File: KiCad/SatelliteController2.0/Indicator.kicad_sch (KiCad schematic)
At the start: 38 parts

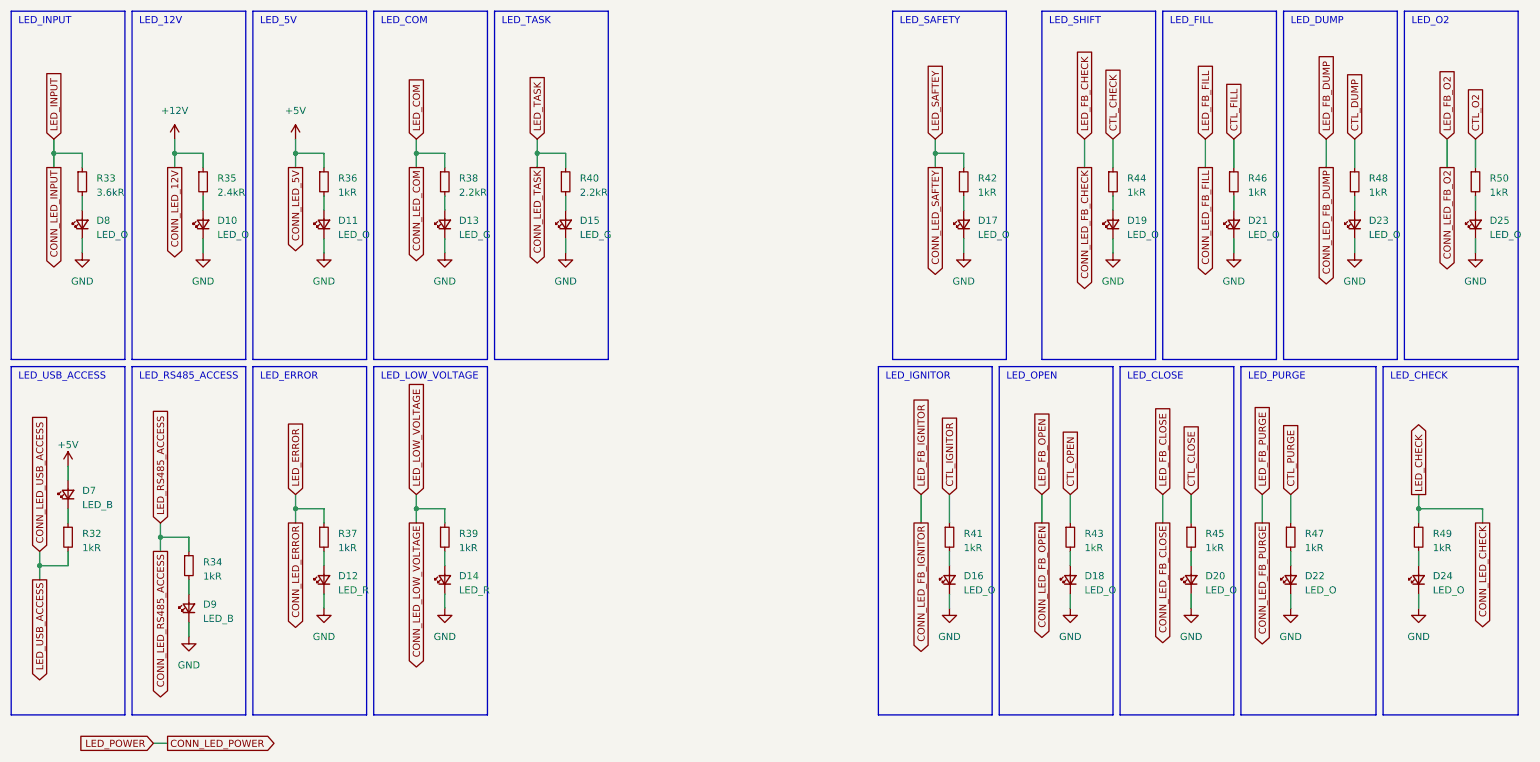
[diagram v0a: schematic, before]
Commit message: シルクなどを調整
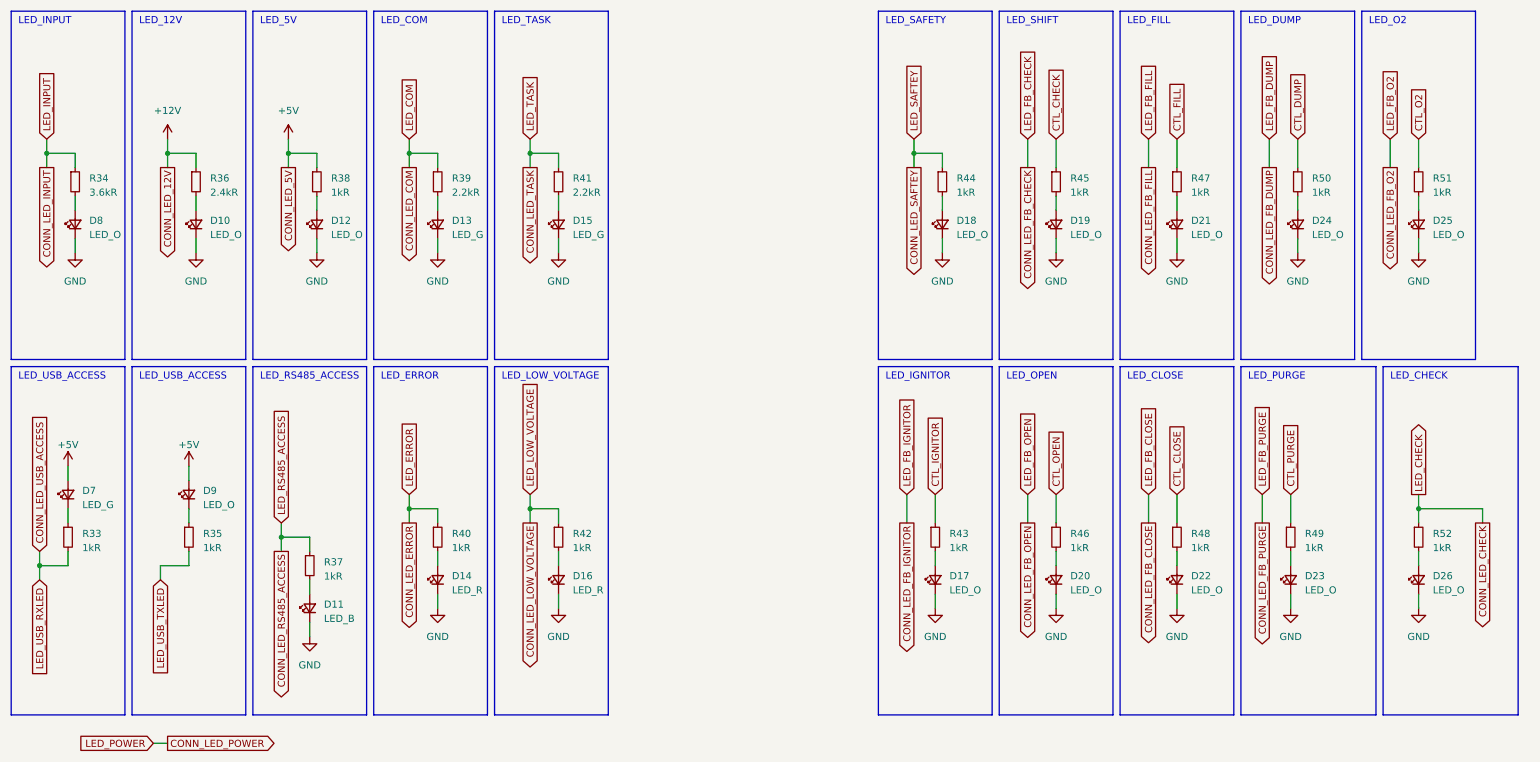
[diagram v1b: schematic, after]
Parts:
- added D9: LED_O, LED_SMD:LED_0603_1608Metric_Pad1.05x0.95mm_HandSolder, symbol Device:LED_Small
- added R35: 1kR, Resistor_SMD:R_0603_1608Metric_Pad0.98x0.95mm_HandSolder, symbol Device:R_Small
- D10, D19, D21, D25, D8: Digikey_PN (none) -> SML-D12D8WT86CCT-ND
- D11: renamed from D9; Digikey_PN (none) -> SMLD12BN1WT86CT-ND
- D12: renamed from D11; Digikey_PN (none) -> SML-D12D8WT86CCT-ND
- D13, D15: Digikey_PN (none) -> SML-D12P8WT86CCT-ND
- D14: renamed from D12; Digikey_PN (none) -> SML-D12U8WT86CCT-ND
- D16: renamed from D14; Digikey_PN (none) -> SML-D12U8WT86CCT-ND
- D17: renamed from D16; Digikey_PN (none) -> SML-D12D8WT86CCT-ND
- D18: renamed from D17; Digikey_PN (none) -> SML-D12D8WT86CCT-ND
- D20: renamed from D18; Digikey_PN (none) -> SML-D12D8WT86CCT-ND
- D22: renamed from D20; Digikey_PN (none) -> SML-D12D8WT86CCT-ND
- D23: renamed from D22; Digikey_PN (none) -> SML-D12D8WT86CCT-ND
- D24: renamed from D23; Digikey_PN (none) -> SML-D12D8WT86CCT-ND
- D26: renamed from D24; Digikey_PN (none) -> SML-D12D8WT86CCT-ND
- D7: value LED_B -> LED_G; Digikey_PN (none) -> SML-D12P8WT86CCT-ND
- R33: renamed from R32; Digikey_PN (none) -> 2019-RK73H1JTTD1001FCT-ND
- R34: renamed from R33; Digikey_PN (none) -> 2019-RK73H1JTTD3601FCT-ND
- R36: renamed from R35; Digikey_PN (none) -> 2019-RK73H1JTTD2401FCT-ND
- R37: renamed from R34; Digikey_PN (none) -> 2019-RK73H1JTTD1001FCT-ND
- R38: renamed from R36; Digikey_PN (none) -> 2019-RK73H1JTTD1001FCT-ND
- R39: renamed from R38; Digikey_PN (none) -> 2019-RK73H1JTTD2201FCT-ND
- R40: renamed from R37; Digikey_PN (none) -> 2019-RK73H1JTTD1001FCT-ND
- R41: renamed from R40; Digikey_PN (none) -> 2019-RK73H1JTTD2201FCT-ND
- R42: renamed from R39; Digikey_PN (none) -> 2019-RK73H1JTTD1001FCT-ND
- R43: renamed from R41; Digikey_PN (none) -> 2019-RK73H1JTTD1001FCT-ND
- R44: renamed from R42; Digikey_PN (none) -> 2019-RK73H1JTTD1001FCT-ND
- R45: renamed from R44; Digikey_PN (none) -> 2019-RK73H1JTTD1001FCT-ND
- R46: renamed from R43; Digikey_PN (none) -> 2019-RK73H1JTTD1001FCT-ND
- R47: renamed from R46; Digikey_PN (none) -> 2019-RK73H1JTTD1001FCT-ND
- R48: renamed from R45; Digikey_PN (none) -> 2019-RK73H1JTTD1001FCT-ND
- R49: renamed from R47; Digikey_PN (none) -> 2019-RK73H1JTTD1001FCT-ND
- R50: renamed from R48; Digikey_PN (none) -> 2019-RK73H1JTTD1001FCT-ND
- R51: renamed from R50; Digikey_PN (none) -> 2019-RK73H1JTTD1001FCT-ND
- R52: renamed from R49; Digikey_PN (none) -> 2019-RK73H1JTTD1001FCT-ND
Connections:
- net +5V: now also D9.2 (A)
- new net: D9.1 (K), R35.1
- new net LED_USB_TXLED: R35.2
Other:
- company: (none) -> Tokai Student Rocket Project
- title: (none) -> Gen6 GSE Satellite Controller 2.0
- moved on the sheet: D10, D11, D12, D13, D14, D15, D16, D17, D18, D19, D20, D21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

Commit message: BOM作成
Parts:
- D10, D12, D17, D18, D19, D20, D21, D22, D23, D24, D25, D26, D8, D9: Digikey_PN SML-D12D8WT86CCT-ND -> SML-D15DWT86CCT-ND
- D11: Digikey_PN SMLD12BN1WT86CT-ND -> SMLD12BN1WT86CT-ND
- D13, D15, D7: Digikey_PN SML-D12P8WT86CCT-ND -> SML-D12P8WT86CCT-ND
- D14, D16: Digikey_PN SML-D12U8WT86CCT-ND -> SML-D12U8WT86CCT-ND
- renumbered R33 to R35, R34 to R36, R35 to R37, R36 to R38, R37 to R39, R38 to R40, R39 to R41, R40 to R42, R41 to R43, R42 to R44, R43 to R45, R44 to R46, R45 to R47, R46 to R48, R47 to R49, R48 to R50, R49 to R51, R50 to R52, R51 to R53, R52 to R54

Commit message: とりあえずプッシュ
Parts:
- D10, D12, D17, D18, D19, D20, D21, D22, D23, D24, D25, D26, D8, D9: DigiKey_PN (none) -> 160-1434-1-ND
- D11: Akiduki_PN (none) -> 103982
- D13, D15, D7: Akiduki_PN (none) -> 111878
- D14, D16: Akiduki_PN (none) -> 111879
- R35, R37, R39, R40, R42, R44, R45, R46, R47, R48, R49, R50, R51, R52, R53, R54: DigiKey_PN (none) -> 2019-RK73H1JTTD1001FCT-ND
- R36: DigiKey_PN (none) -> 2019-RK73H1JTTD3601FCT-ND
- R38: DigiKey_PN (none) -> 2019-RK73H1JTTD2401FCT-ND
- R41, R43: DigiKey_PN (none) -> 2019-RK73H1JTTD2201FCT-ND
